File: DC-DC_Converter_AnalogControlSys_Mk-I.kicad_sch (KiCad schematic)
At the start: 32 parts, among them J1 Conn_01x06, J2 TRIAmpTestPoint, J3 SQRTestPoint, J4 Conn_01x03, U1 TL054CN, U2 TL054CN

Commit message: ADDED all LCSC part numbers and footprints. FIXED schematic (and model) to use a smaller range of resistor and capacitor values to increase cost efficiency, at the expense of control system performance. TODO begin designing PCB.
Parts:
- removed R14: 13k, symbol Device:R_US
- removed R3: 30k, symbol Device:R_US
- added R17: 1k, PCM_Resistor_SMD_AKL:R_0603_1608Metric_Pad0.98x0.95mm, symbol Device:R_US
- added R19, R20, R21, R22, R23, R24: 10k, PCM_Resistor_SMD_AKL:R_0805_2012Metric_Pad1.15x1.40mm, symbol Device:R_US
- added R25, R26: 2.2k, PCM_Resistor_SMD_AKL:R_0603_1608Metric_Pad0.98x0.95mm, symbol Device:R_US
- C1: renamed from C3; value 8.2n -> 10n; footprint (none) -> PCM_Capacitor_SMD_AKL:C_0805_2012Metric_Pad1.15x1.40mm; LCSC Part # (none) -> C52278
- C2: renamed from C7; footprint (none) -> PCM_Capacitor_SMD_AKL:C_0805_2012Metric_Pad1.15x1.40mm; LCSC Part # (none) -> C520083
- C3: renamed from C2; footprint (none) -> PCM_Capacitor_SMD_AKL:C_0805_2012Metric_Pad1.15x1.40mm; LCSC Part # (none) -> C520083
- C4: renamed from C1; footprint (none) -> PCM_Capacitor_SMD_AKL:C_0805_2012Metric_Pad1.15x1.40mm; LCSC Part # (none) -> C52278
- C5: renamed from C4; value 3.3u -> 2.2u; footprint (none) -> PCM_Capacitor_SMD_AKL:C_0603_1608Metric_Pad1.05x0.95mm; LCSC Part # (none) -> C415535; now left out of the parts list
- J1: footprint (none) -> Connector_PinHeader_2.54mm:PinHeader_1x06_P2.54mm_Vertical; LCSC Part # (none) -> N/A; now left out of the parts list
- J2: renamed from J4; footprint (none) -> Connector_PinHeader_2.54mm:PinHeader_1x03_P2.54mm_Vertical; LCSC Part # (none) -> N/A; now left out of the parts list
- J3: renamed from J2; LCSC Part # (none) -> N/A; now left out of the parts list
- J4: renamed from J3; LCSC Part # (none) -> N/A; now left out of the parts list
- R1: renamed from R2; footprint (none) -> PCM_Resistor_SMD_AKL:R_0805_2012Metric_Pad1.15x1.40mm; LCSC Part # (none) -> C212284
- R10: renamed from R16; footprint (none) -> PCM_Resistor_SMD_AKL:R_0603_1608Metric_Pad0.98x0.95mm; LCSC Part # (none) -> C423061
- R11: renamed from R13; footprint (none) -> PCM_Resistor_SMD_AKL:R_0805_2012Metric_Pad1.15x1.40mm; LCSC Part # (none) -> C966565
- R12: renamed from R7; footprint (none) -> PCM_Resistor_SMD_AKL:R_0805_2012Metric_Pad1.15x1.40mm; LCSC Part # (none) -> C212284
- R13: renamed from R11; footprint (none) -> PCM_Resistor_SMD_AKL:R_0603_1608Metric_Pad0.98x0.95mm; LCSC Part # (none) -> C209012
- R14: renamed from R9; footprint (none) -> PCM_Resistor_SMD_AKL:R_0603_1608Metric_Pad0.98x0.95mm; LCSC Part # (none) -> C209012
- R15: renamed from R5; footprint (none) -> PCM_Resistor_SMD_AKL:R_0805_2012Metric_Pad1.15x1.40mm; LCSC Part # (none) -> C212284
- R16: renamed from R10; footprint (none) -> PCM_Resistor_SMD_AKL:R_0603_1608Metric_Pad0.98x0.95mm; LCSC Part # (none) -> C209012
- R18: value 12k -> 10k; footprint (none) -> PCM_Resistor_SMD_AKL:R_0805_2012Metric_Pad1.15x1.40mm; LCSC Part # (none) -> C212284
- R2: renamed from R19; footprint (none) -> PCM_Resistor_SMD_AKL:R_0805_2012Metric_Pad1.15x1.40mm; LCSC Part # (none) -> C212284
- R3: renamed from R4; footprint (none) -> PCM_Resistor_SMD_AKL:R_0805_2012Metric_Pad1.15x1.40mm; LCSC Part # (none) -> C212284
- R4: renamed from R1; footprint (none) -> PCM_Resistor_SMD_AKL:R_0603_1608Metric_Pad0.98x0.95mm; LCSC Part # (none) -> C209012
- R5: renamed from R17; footprint (none) -> PCM_Resistor_SMD_AKL:R_0603_1608Metric_Pad0.98x0.95mm; LCSC Part # (none) -> C209012
- R6: value 30k -> 10k; footprint (none) -> PCM_Resistor_SMD_AKL:R_0805_2012Metric_Pad1.15x1.40mm; LCSC Part # (none) -> C212284
- R7: renamed from R15; footprint (none) -> PCM_Resistor_SMD_AKL:R_0603_1608Metric_Pad0.98x0.95mm; LCSC Part # (none) -> C423061
- R8: footprint (none) -> PCM_Resistor_SMD_AKL:R_0805_2012Metric_Pad1.15x1.40mm; LCSC Part # (none) -> C212284
- R9: renamed from R12; value 5k -> 5.1k; footprint (none) -> PCM_Resistor_SMD_AKL:R_0603_1608Metric_Pad0.98x0.95mm; LCSC Part # (none) -> C318133; now left out of the parts list
- RV1, RV2: LCSC Part # (none) -> C48997914
- U1, U2: footprint PCM_Package_DIP_AKL:DIP-14_W7.62mm_LongPads -> Package_DIP:DIP-14_W7.62mm; LCSC Part # (none) -> C1347256
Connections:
- net -5V: now also R21.1
- net GND: now also R19.2
- net targ_in: now also R22.2; no longer R6.2
- net at R15.1, U2.7: now also R25.2; no longer R18.1
- net at R18.2, U2.6 (-): now also R24.1; no longer R6.1
- net at R11.2, U1.12 (+): now also R17.2
- net at C3.2, R3.1, U1.10 (+): now also R6.2
- new net: R23.1, R24.2
- new net: R22.1, R23.2
- new net: R19.1, R26.1
- new net: R17.1, R26.2
- new net: R18.1, R25.1
- new net: R20.2, R6.1
- new net: R20.1, R21.2
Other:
- note removed: "TODO: define and assign netclasses"
- note removed: "TODO: start assigning LCSC part numbers"
- moved on the sheet: J1

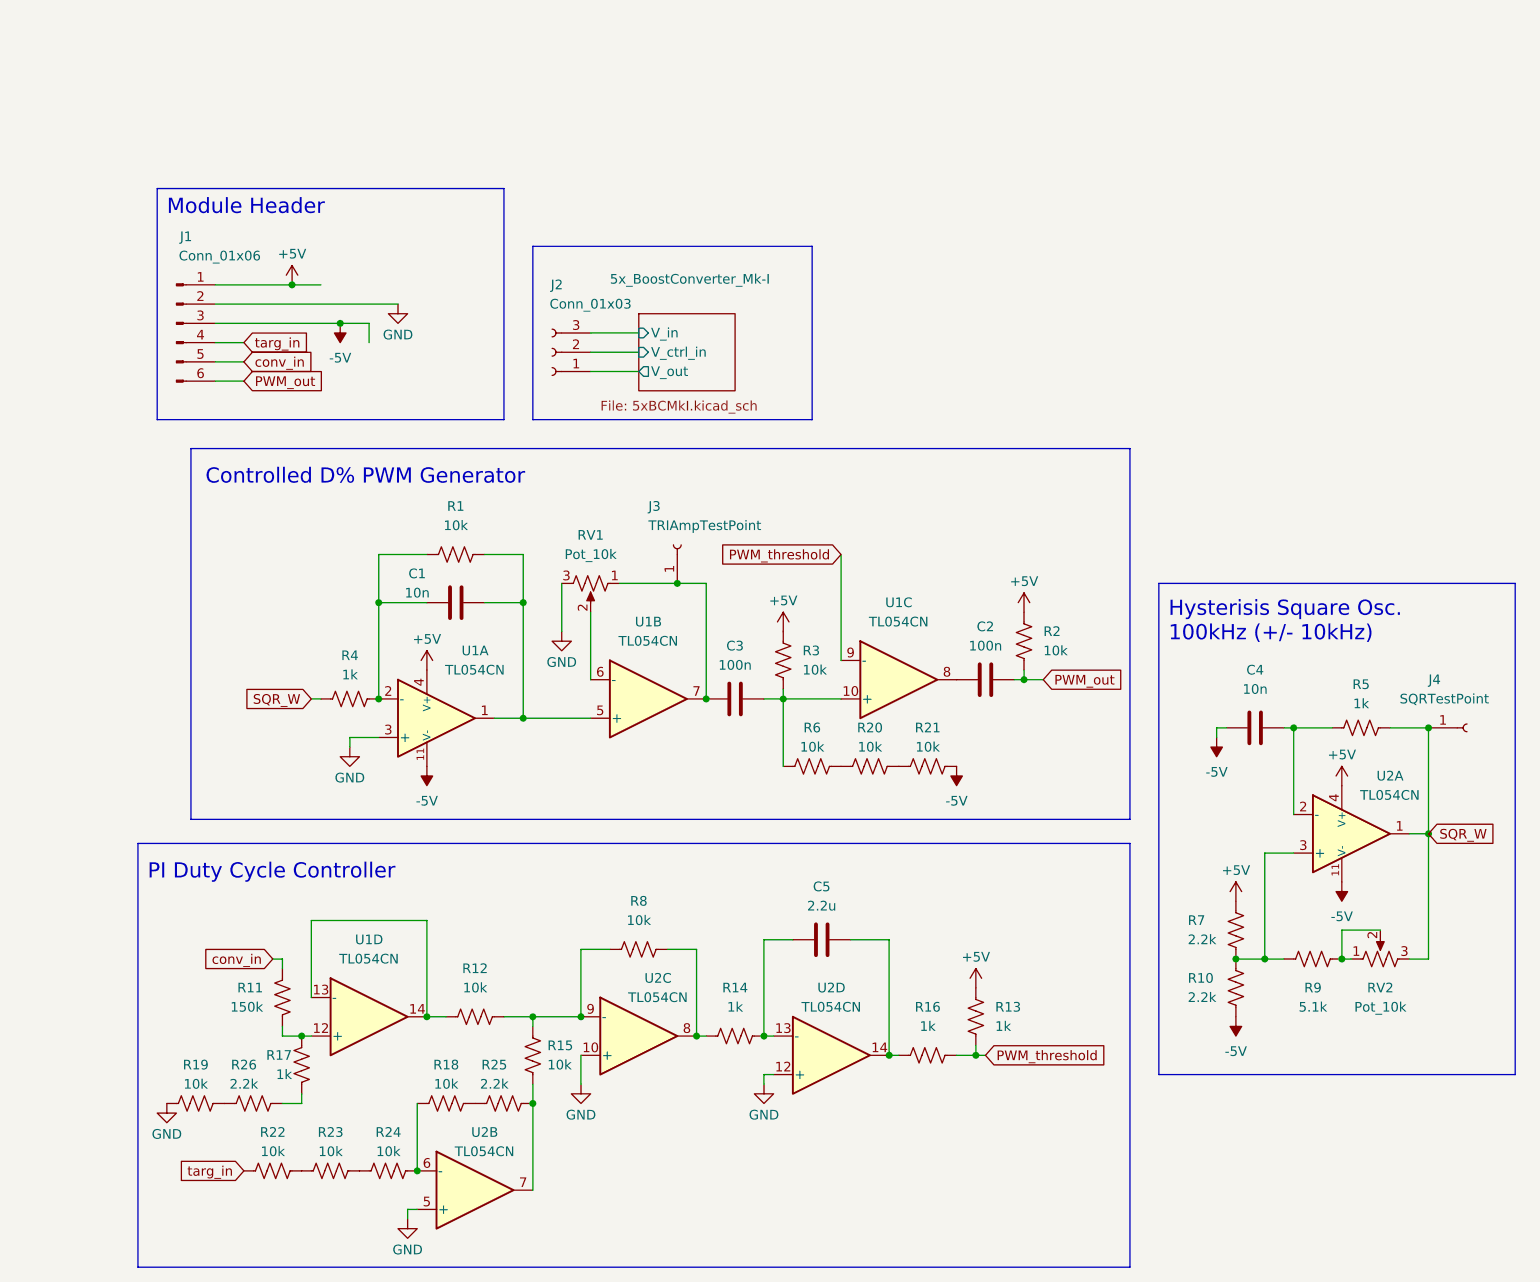
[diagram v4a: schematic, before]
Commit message: Finalized design files for assembly and organized BOM.
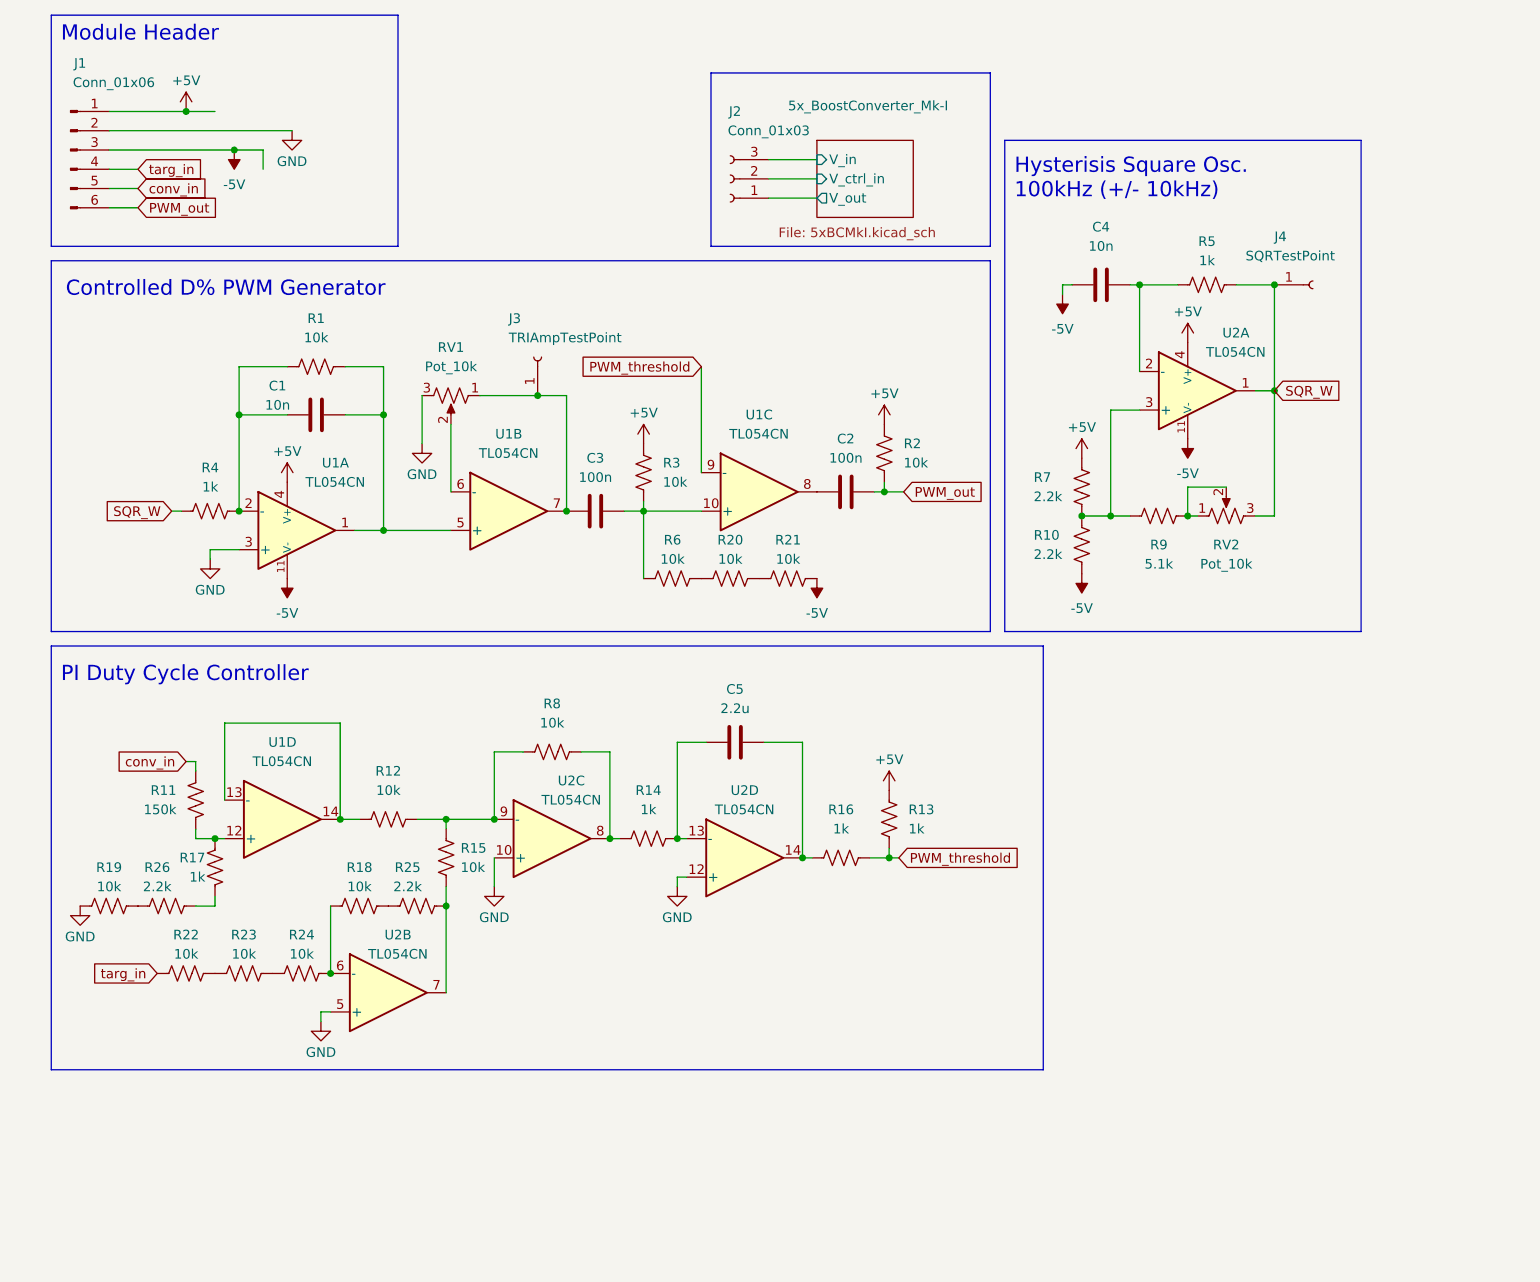
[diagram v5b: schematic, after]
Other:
- moved on the sheet: C1, C2, C3, C4, C5, J1, J2, J3, J4, R1, R10, R11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
